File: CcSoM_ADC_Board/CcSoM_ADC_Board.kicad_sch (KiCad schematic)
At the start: 17 parts, among them J1 SoM Connector, U1 SN74LVC00APWE4, U2 74AUP1G04

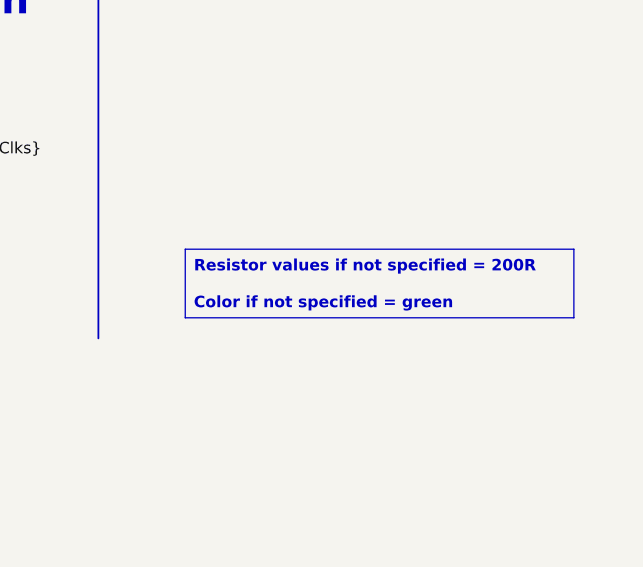
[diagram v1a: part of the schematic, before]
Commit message: corrected schematic created pdf and bom file
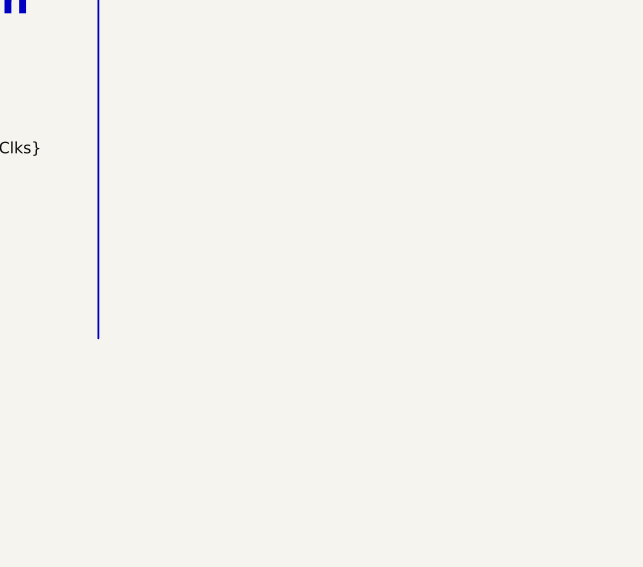
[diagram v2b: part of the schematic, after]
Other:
- title: SoM Programmer & Tester -> SoM Programmer & ADC Board
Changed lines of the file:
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@@
 	(paper "A4")
 	(title_block
-		(title "SoM Programmer & Tester")
-		(date "2024-12-20")
+		(title "SoM Programmer & ADC Board")
+		(date "2026-02-09")
 		(rev "0.1")
 		(company "Technische Hochschule Köln")
 		(comment 1 "Felix Sebastian Nitz")
+		(comment 2 "Ismail Özdemirkan")
 	)
 	(bus_alias "User_Clks"
@@
 		)
 	)
-	(text_box "Resistor values if not specified = 200R\n\nColor if not specified = green"
-		(exclude_from_sim no)
-		(at 240.03 156.21 0)
-		(size 43.18 7.62)
-		(margins 0.9525 0.9525 0.9525 0.9525)
-		(stroke
-			(width 0)
-			(type default)
-		)
-		(fill
-			(type none)
-		)
-		(effects
-			(font
-				(size 1.27 1.27)
-				(thickness 0.254)
-				(bold yes)
-			)
-			(justify left)
-		)
-	)

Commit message: changed schottky, began to add digikey part numbers
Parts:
- U1: DigiKey_no (none) -> SN74LVC00APWE4-ND
- U2: DigiKey_no (none) -> 296-SN74AUP1G04DBVRCT-ND
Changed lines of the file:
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@@
+			)
+		)
+		(property "DigiKey_no" "SN74LVC00APWE4-ND"
+			(at 36.83 129.54 0)
+			(effects
+				(font
+					(size 1.27 1.27)
+				)
+				(hide yes)
 			)
 		)
@@
 			)
 		)
+		(property "DigiKey_no" "SN74LVC00APWE4-ND"
+			(at 134.62 137.16 0)
+			(effects
+				(font
+					(size 1.27 1.27)
+				)
+				(hide yes)
+			)
+		)
 		(pin "6"
 		)
@@
 			)
 		)
+		(property "DigiKey_no" "296-SN74AUP1G04DBVRCT-ND"
+			(at 110.49 134.62 0)
+			(effects
+				(font
+					(size 1.27 1.27)
+				)
+				(hide yes)
+			)
+		)
 		(pin "5"
 		)
@@
 				)
 				(justify left top)
+				(hide yes)
+			)
+		)
+		(property "DigiKey_no" "SN74LVC00APWE4-ND"
+			(at 27.94 175.26 0)
+			(effects
+				(font
+					(size 1.27 1.27)
+				)
 				(hide yes)
 			)
@@
 			)
 		)
+		(property "DigiKey_no" "SN74LVC00APWE4-ND"
+			(at 36.83 142.24 0)
+			(effects
+				(font
+					(size 1.27 1.27)
+				)
+				(hide yes)
+			)
+		)
 		(pin "6"
 		)
@@
 				(hide yes)
 			)
+		)
+		(property "DigiKey_no" "SN74LVC00APWE4-ND"
+			(at 134.62 151.13 0)
+			(effects
+				(font
+					(size 1.27 1.27)
+				)
+				(hide yes)
+			)

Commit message: digikey no not complete
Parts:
- D1, D2: DigiKey_no (none) -> 4878-1N4148WTCT-ND
- D3: DigiKey_no (none) -> 732-4979-1-ND
- D4: DigiKey_no (none) -> 732-4980-1-ND
- J1: DigiKey_no (none) -> A121565-ND
- JP1, JP2: DigiKey_no (none) -> 664-G800W306018EU-ND
- R1, R3: DigiKey_no (none) -> 311-200HRCT-ND
- R2: DigiKey_no (none) -> 541-47.0KHCT-ND
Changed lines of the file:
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@@
 			)
 		)
+		(property "DigiKey_no" "A121565-ND"
+			(at 69.85 82.55 0)
+			(effects
+				(font
+					(size 1.27 1.27)
+				)
+				(hide yes)
+			)
+		)
 		(pin "13"
 		)
@@
 			)
 		)
+		(property "DigiKey_no" "732-4979-1-ND"
+			(at 72.39 139.7 0)
+			(effects
+				(font
+					(size 1.27 1.27)
+				)
+				(hide yes)
+			)
+		)
 		(pin "1"
 		)
@@
 			)
 		)
+		(property "DigiKey_no" "4878-1N4148WTCT-ND"
+			(at 63.5 48.26 0)
+			(effects
+				(font
+					(size 1.27 1.27)
+				)
+				(hide yes)
+			)
+		)
 		(pin "1"
 		)
@@
 			)
 		)
+		(property "DigiKey_no" "311-200HRCT-ND"
+			(at 157.48 137.16 90)
+			(effects
+				(font
+					(size 1.27 1.27)
+				)
+				(hide yes)
+			)
+		)
 		(pin "2"
 		)
@@
 			)
 		)
+		(property "DigiKey_no" "311-200HRCT-ND"
+			(at 66.04 133.35 90)
+			(effects
+				(font
+					(size 1.27 1.27)
+				)
+				(hide yes)
+			)
+		)
 		(pin "2"
 		)
@@
 			)
 		)
+		(property "DigiKey_no" "541-47.0KHCT-ND"
+			(at 85.09 33.02 0)
+			(effects
+				(font
+					(size 1.27 1.27)
+				)
+				(hide yes)
+			)
+		)
 		(pin "2"
 		)
@@
 			)
 		)
+		(property "DigiKey_no" "664-G800W306018EU-ND"
+			(at 25.4 77.47 90)
+			(effects
+				(font
+					(size 1.27 1.27)
+				)
+				(hide yes)
+			)
+		)
 		(pin "1"
 		)
@@
 			)
 		)
+		(property "DigiKey_no" "732-4980-1-ND"
+			(at 165.1 142.24 0)
+			(effects
+				(font
+					(size 1.27 1.27)
+				)
+				(hide yes)
+			)
+		)
 		(pin "1"
 		)
@@
 			)
 		)
+		(property "DigiKey_no" "A121565-ND"
+			(at 157.48 62.23 90)
+			(effects
+				(font
+					(size 1.27 1.27)
+				)
+				(hide yes)
+			)
+		)
 		(pin "13"
 		)
@@
 			)
 		)
+		(property "DigiKey_no" "664-G800W306018EU-ND"
+			(at 19.05 77.47 90)
+			(effects
+				(font
+					(size 1.27 1.27)
+				)
+				(hide yes)
+			)
+		)
 		(pin "1"
 		)
@@
 			(at 64.77 31.75 0)
 			(effects
+				(font
+					(size 1.27 1.27)
+				)
+				(hide yes)
+			)
+		)
+		(property "DigiKey_no" "4878-1N4148WTCT-ND"
+			(at 64.77 31.75 0)
+			(effects

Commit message: corrected differential pairs
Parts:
- log2: value ~ -> (none)
